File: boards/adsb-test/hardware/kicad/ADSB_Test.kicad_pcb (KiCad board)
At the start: 4 copper layers, 180.9 x 116 mm, 493 parts, among them J1001 Dev USB-C, J1101 USB-A (SDR hub), J1201 SMA GNSS (active antenna), J1301 LCD FPC 30p 0.5mm, J1302 Touch FPC 6p 0.5mm, J1401 m1421 JTAG (J-Link), J1402 ADSBee 1421 Dev Kit, J1403 SMA 1090/978, J1501 microSD (push-pull, detect), J1601 Kingst LA5016 (2x20 keyed), J1801 RP2040 GPIO (pins DNP), J301 2S Li-ion pack (BAT+, GND, NT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, J801 HR911105A, J901 User USB-C (PD sink + UART), Q1501 AO3401A, Q1701 MMBT3904, Q1702 MMBT3904, Q1703 MMBT3904, Q1704 MMBT3904, Q201 FDS9435A, SW1801 BOOTSEL (programmer), SW401 POWER (slide), SW601 BOOT, SW602 RESET, U1001 USBLC6-2SC6, U1002 AP2112K-3.3, U1003 USB2514B, U1101 TPS259621DDA, U1102 USBLC6-2SC6, U1201 MAX-M10S, U1301 AP3012KTR-E1, U1302 AP2112K-1.8, U1303 AP3032KTR-G1, U1401 ADSBee m1421, U1402 74LVC1G97 (AND), U1403 74LVC1G32, U1404 74LVC1G07, U1405 SCN-2-11+, U1501 TCA6408APW, U1701 FT2232HL, U1702 93LC56B, U1703 74LVC1G07, U1704 74LVC1G125, U1705 74LVC1G07, U1706 74LVC1G125, U1801 RP2040, U1802 W25Q16JVSS, U1803 74LVC1G125, U1804 74LVC1G125, U1805 74LVC1G125, U1806 74LVC1G125, U201 STUSB4500QTR, U301 BQ25798, U302 MCP1703 3.0V (2 uA Iq), U411 TPS62933, U421 TPS62933, U430 TPS22917, U431 TPS22917, U432 TPS22917, U433 TPS22917, U501 PAC1954 (PM1), U502 PAC1954 (PM2), U503 PAC1954 (PM3), U601 ESP32-P4C5 Core (OSPTEK), U701 DS3231M, U801 LAN8720A, U901 CP2102N-A02-GQFN24, U902 USBLC6-2SC6, Y1001 24MHz, Y1701 12MHz, Y1801 12MHz, Y601 32.768kHz, Y801 25MHz

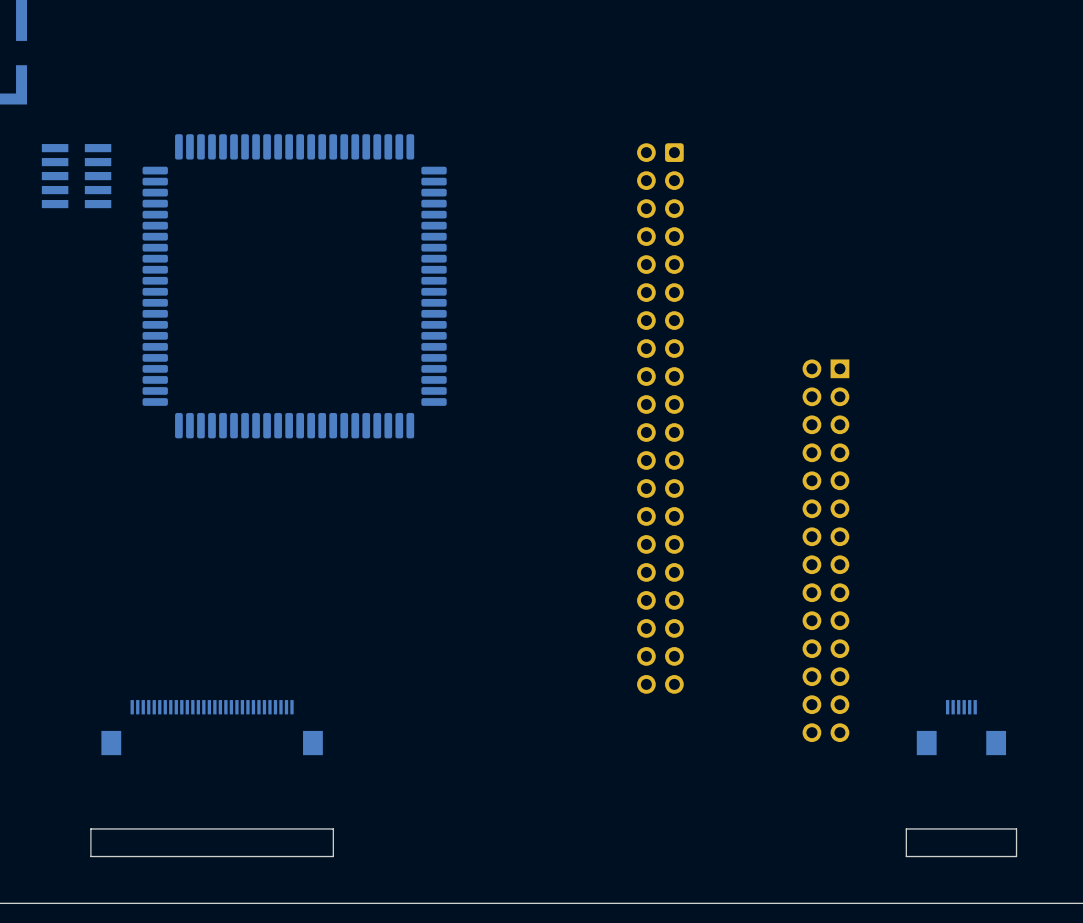
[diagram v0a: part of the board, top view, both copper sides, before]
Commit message: ADSB_Test PCB: panel FPC slots moved to the panel drawing positions
Co-Authored-By: Claude Opus 5.5 <noreply@anthropic.com>
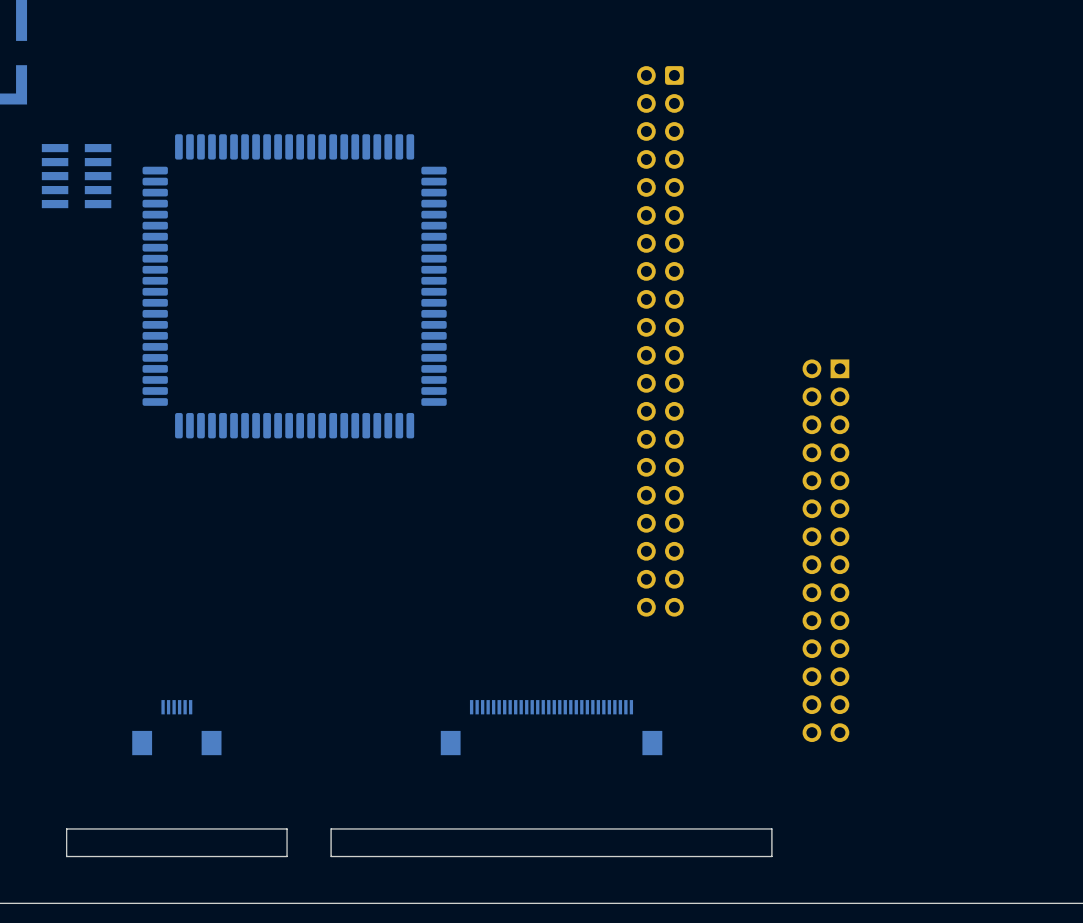
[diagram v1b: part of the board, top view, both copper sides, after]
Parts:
- moved J1302 71.2 mm to (150.0, 200.1)
- moved J1301 30.8 mm to (184.0, 200.1)
- moved J1601 7.00 mm to (195.2, 140.9)
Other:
- outline, holes or cut-outs redrawn

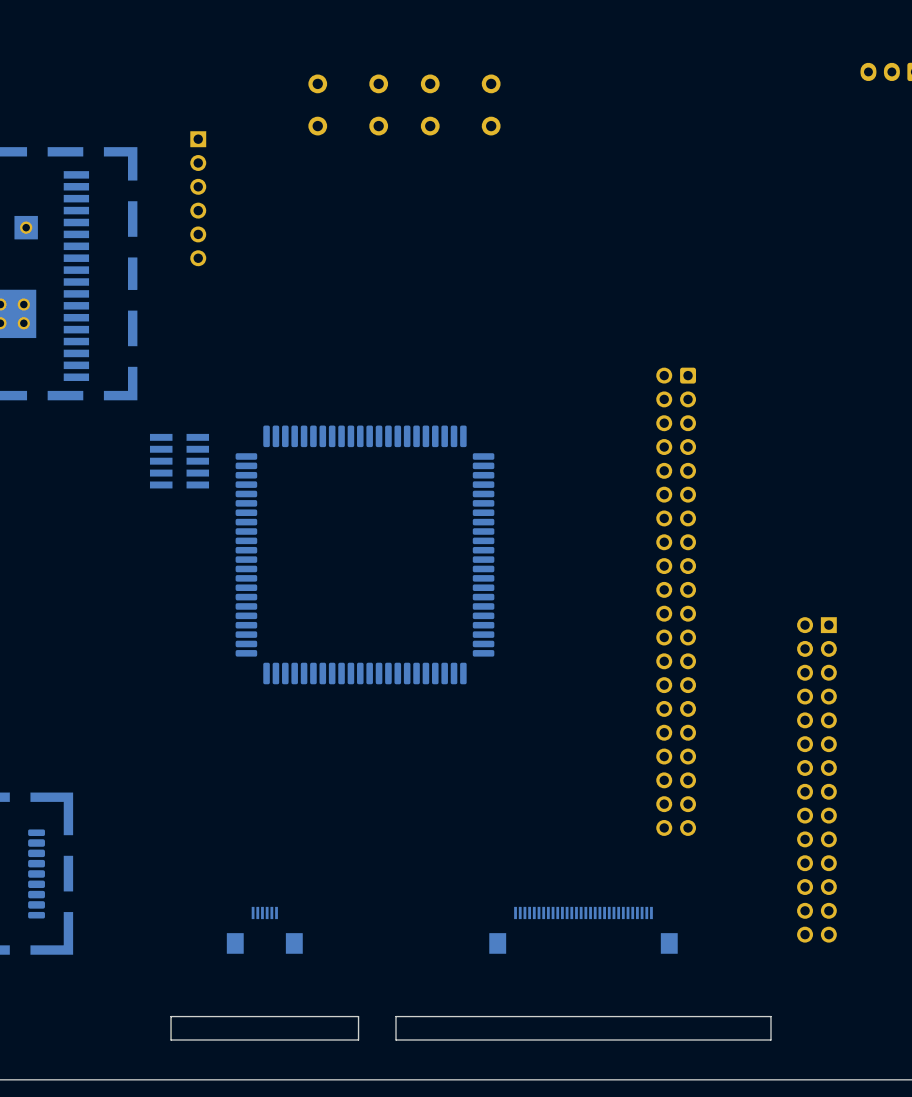
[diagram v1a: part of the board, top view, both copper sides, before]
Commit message: ADSB_Test PCB: FPC slots and sockets moved into the middle, past the tail chip section
Co-Authored-By: Claude Opus 5.5 <noreply@anthropic.com>
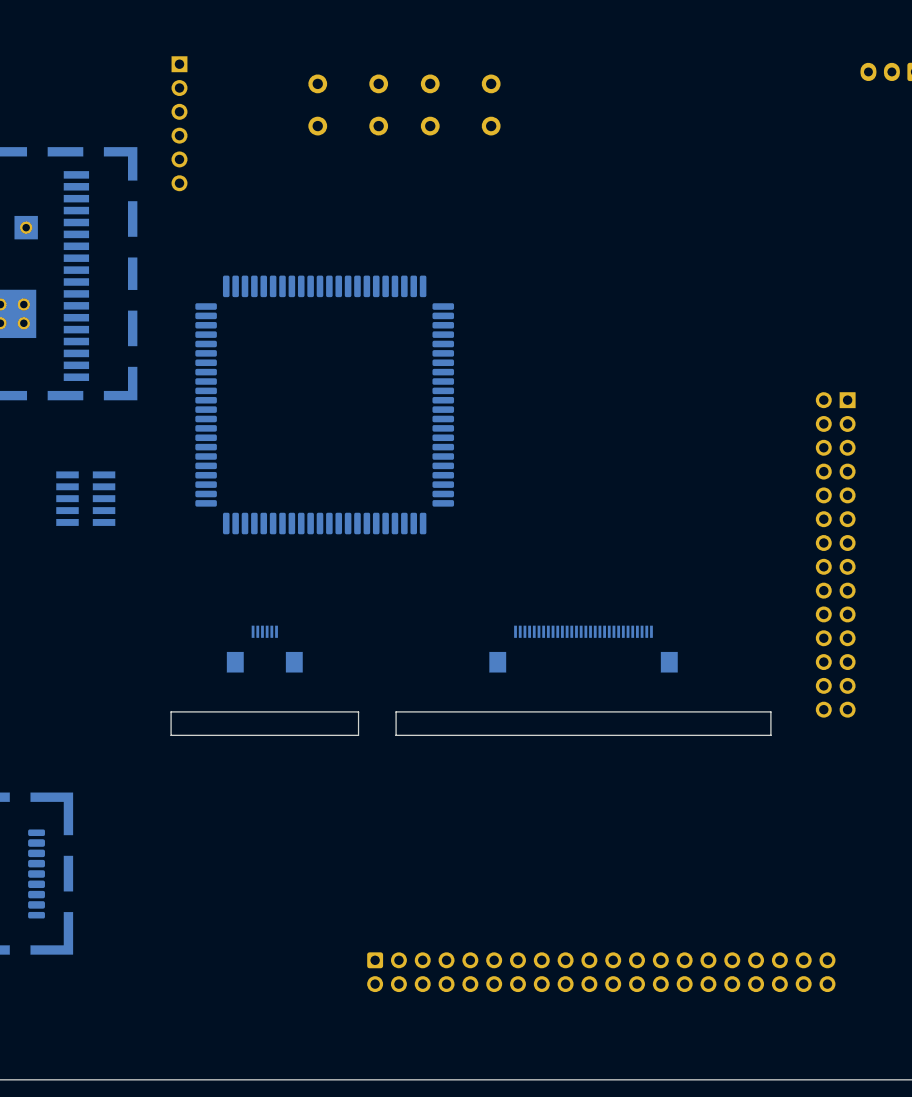
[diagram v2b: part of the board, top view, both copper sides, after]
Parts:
- moved J1601 70.7 mm to (161.8, 203.2), turned to -90 degrees
- moved J1301 30.0 mm to (184.0, 170.1)
- moved J1302 30.0 mm to (150.0, 170.1)
- moved J1801 24.1 mm to (212.2, 143.5)
- moved U601 16.6 mm to (156.4, 144.0)
- moved J1401 10.8 mm to (130.9, 154.0)
- moved J1402 8.25 mm to (140.9, 107.7)
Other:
- outline, holes or cut-outs redrawn

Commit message: ADSB_Test: SLEEP/WAKE button on GPIO12 with BSP deep-sleep support
SW603 right-angle tactile on the digital edge next to POWER, 10k pull-up on
3V3_MCU, 470R + 100nF. bsp_sleep() turns the expander rails off, holds the C5
in reset and deep-sleeps the P4 with ext1 wake on the button (and optionally
the DS3231M alarm). [sleep] test, BOM line, docs, PCB regenerated.

Co-Authored-By: Claude Opus 5.5 <noreply@anthropic.com>
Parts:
- added C609: 100nF, Capacitor_SMD:C_0805_2012Metric_Pad1.18x1.45mm_HandSolder, B.Cu at (342.7, 351.0)
- added R608: 10k, Resistor_SMD:R_0805_2012Metric_Pad1.20x1.40mm_HandSolder, B.Cu at (313.5, 354.9)
- added R609: 470R, Resistor_SMD:R_0805_2012Metric_Pad1.20x1.40mm_HandSolder, B.Cu at (318.8, 354.9)
- added SW603: SLEEP/WAKE, Button_Switch_THT:SW_Tactile_SPST_Angled_PTS645Vx31-2LFS, B.Cu at (277.7, 205.5)
- TP608: value P4_GPIO12 -> SLEEP_WAKE
- moved R605 66.0 mm to (297.8, 354.9)
- moved Y601 55.2 mm to (298.7, 358.7)
- moved TP601 15.8 mm to (323.4, 355.2)
- moved TP602 15.8 mm to (327.5, 355.2)
- moved TP603 15.8 mm to (331.5, 355.2)
- moved TP604 15.8 mm to (335.6, 355.2)
- moved TP605 15.8 mm to (339.6, 355.2)
- moved TP606 15.8 mm to (343.7, 355.2)
- moved TP607 15.8 mm to (347.7, 355.2)
- moved TP608 15.8 mm to (351.8, 355.2)
- moved TP609 15.8 mm to (355.8, 355.2)
- moved TP610 15.8 mm to (359.9, 355.2)
- moved TP611 15.8 mm to (363.9, 355.2)
- moved SW401 10.9 mm to (274.2, 189.4)
- moved J1501 8.73 mm to (274.3, 177.5)
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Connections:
- net /MCU Module/P4_GPIO12 renamed /MCU Module/SLEEP_WAKE
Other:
- board text added: "[MCU Module] 30 parts"
- board text removed: "[MCU Module] 27 parts"
